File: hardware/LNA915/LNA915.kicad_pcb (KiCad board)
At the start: 4 copper layers, 38 x 7.8 mm, 32 parts, among them P1 HACKRF, P2 ANTENNA, U1 SWITCH, U2 SAW, U3 LNA

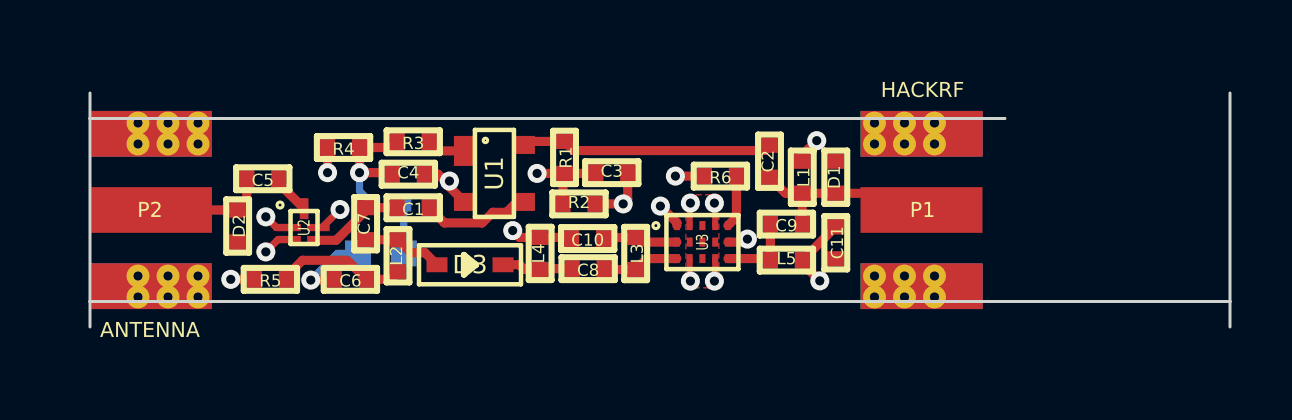
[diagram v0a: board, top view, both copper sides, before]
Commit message: LNA915: correct minor layout errors
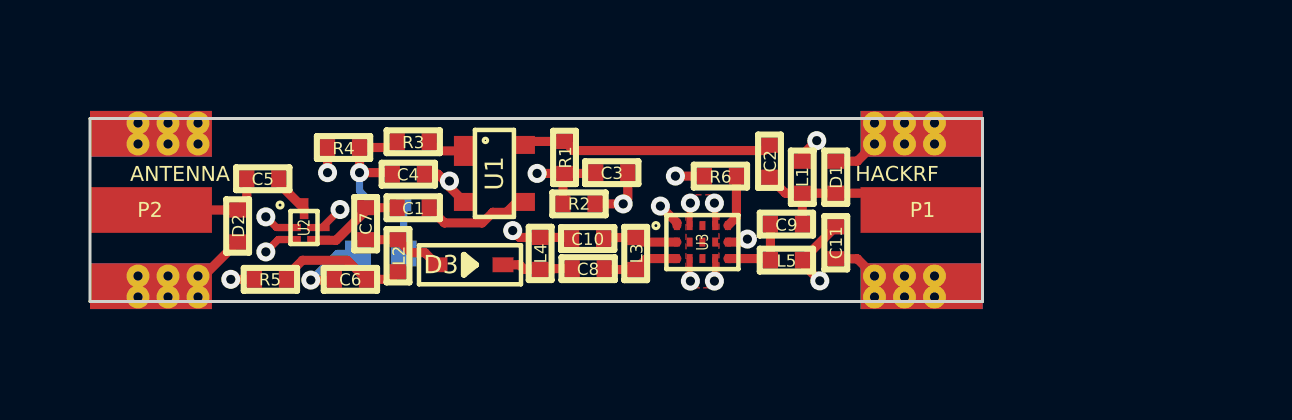
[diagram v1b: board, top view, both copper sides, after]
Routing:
- net GND: track 15.5 -> 21.3 mm
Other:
- board size 38 x 7.8 mm -> 29.8 x 6.1 mm
- board text added: "21 Jun 2020"
- board text added: "https://greatscottgadgets.com/"
- board text removed: "11 Jan 2016"
- board text removed: "http://greatscottgadgets.com/hackrf/"

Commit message: LNA915: redesign around GRF6011 failsafe switch
fits in SMA-KIT-1.5MF inline SMA enclosure
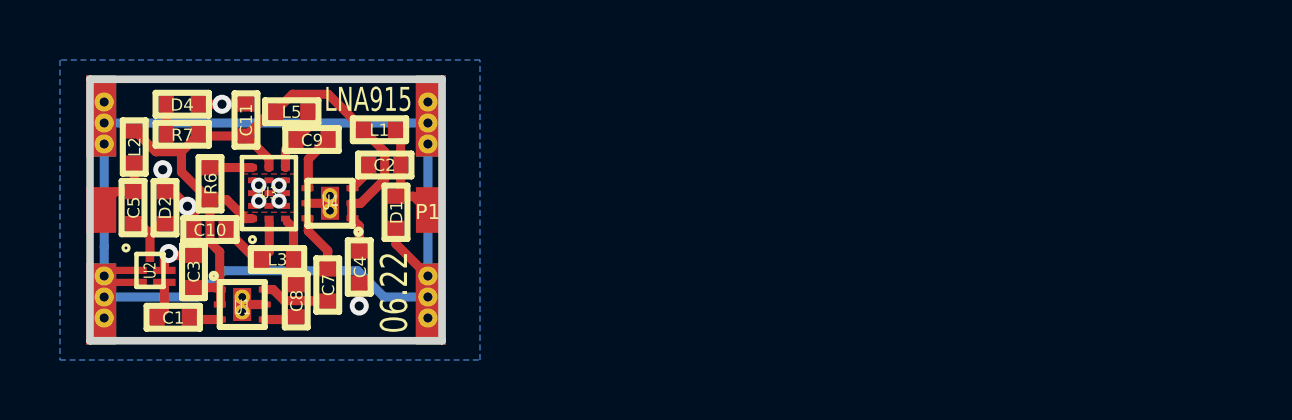
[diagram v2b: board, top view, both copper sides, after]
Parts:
- removed C6: 1nF, gsg-modules:0402
- removed D3: PIN, hackrf:GSG-SOD323
- removed L4: 39nH, gsg-modules:0402
- removed P2: ANTENNA, gsg-modules:SMA-EDGE
- removed R1: 47k, gsg-modules:0402
- removed R2, R4: 100k, gsg-modules:0402
- removed R3: 4k7, gsg-modules:0402
- removed R5: 470, gsg-modules:0402
- added U4: SWITCH, LNA915:GRF6011, F.Cu at (133.0, 99.8)
- C3, C4: value 1nF -> 100pF
- D4: footprint gsg-modules:0603D -> gsg-modules:0402; moved to F.Cu
- P1: value HACKRF -> SMA-KIT-1.5MF; footprint gsg-modules:SMA-EDGE -> LNA915:SMA-KIT-1.5MF
- R7: moved to F.Cu
- U1: footprint hackrf:GSG-SOT143 -> LNA915:GRF6011
- moved C11 20.1 mm to (130.2, 97.0), turned to 270 degrees
- moved P1 17.9 mm to (136.9, 100.0)
- moved L5 17.2 mm to (131.7, 96.7), turned to 0 degrees
- moved R6 17.0 mm to (129.0, 99.1), turned to 90 degrees
- moved C9 16.1 mm to (132.4, 97.7)
- moved D1 14.7 mm to (135.2, 100.1), turned to 90 degrees
- moved U3 14.5 mm to (131.0, 99.4), turned to 0 degrees
- moved C3 14.3 mm to (128.4, 102.0), turned to 270 degrees
- moved L1 14.2 mm to (134.7, 97.3), turned to 180 degrees
- moved C2 12.8 mm to (134.8, 98.5), turned to 0 degrees
- moved C10 12.6 mm to (129.0, 100.7)
- moved L3 11.9 mm to (131.2, 101.7), turned to 180 degrees
- moved C8 9.79 mm to (131.9, 103.0), turned to 90 degrees
- moved L2 9.51 mm to (126.5, 97.9), turned to 90 degrees
- moved U1 9.47 mm to (130.1, 103.2), turned to 0 degrees
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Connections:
- C7 pad 1: Net-(C1-Pad1) -> Net-(C7-Pad1)
- C9 pad 2: Net-(C2-Pad2) -> Net-(C9-Pad2)
- D2 pad 2: Net-(C5-Pad1) -> Net-(C5-Pad2)
- D4 pad 1: Net-(D4-Pad1) -> GND
- D4 pad 2: GND -> Net-(D4-Pad2)
- L2 pad 1: Net-(C7-Pad2) -> Net-(C5-Pad1)
- L2 pad 2: Net-(C6-Pad2) -> VCC
- R7 pad 2: Net-(D4-Pad1) -> Net-(D4-Pad2)
- U1 pad 1: Net-(R3-Pad2) -> VCC
- U1 pad 2: GND -> VCC
- U1 pad 4: Net-(C2-Pad1) -> Net-(C8-Pad1)
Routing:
- net GND: track 21.3 -> 51.5 mm, vias 12 -> 9
- net VCC: track 14.0 -> 24.0 mm, vias 8 -> 0
- net Net-(C2-Pad1): track 8.42 -> 1.01 mm
- net Net-(C6-Pad2): track 4.41 -> 0.00 mm
- net Net-(C2-Pad2): track 6.56 -> 3.67 mm
- net Net-(C1-Pad2): track 3.67 -> 1.07 mm
- net Net-(C7-Pad1): track 0.00 -> 2.29 mm
- net Net-(C1-Pad1): track 3.13 -> 1.15 mm
- net Net-(C9-Pad2): track 0.00 -> 1.90 mm
- net Net-(C5-Pad1): track 4.06 -> 2.35 mm
- net Net-(D4-Pad1): track 1.68 -> 0.00 mm
- net Net-(C8-Pad1): track 2.42 -> 1.11 mm
- net Net-(R3-Pad2): track 1.30 -> 0.00 mm
- net Net-(D4-Pad2): track 0.00 -> 1.00 mm
- net Net-(C7-Pad2): track 2.72 -> 1.96 mm
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- added copper zone on B.Cu, net GND
- removed copper zone on C2, net GND
- removed copper zone on C3, net VCC
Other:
- board size 29.8 x 6.1 mm -> 11.7 x 8.7 mm
- copper layers 4 -> 2
- net class Default: clearance 0.1524 -> 0.127
- rule pad_to_mask_clearance: 0.0762 -> 0.0508
- rule trace_clearance: 0.1524 -> 0.127
- board text added: "06.22"
- board text added: "RX"
- board text added: "TX"
- board text removed: "21 Jun 2020"
- board text removed: "LNA"
- board text removed: "P1"
- board text removed: "P2"
- board text removed: "https://greatscottgadgets.com/"

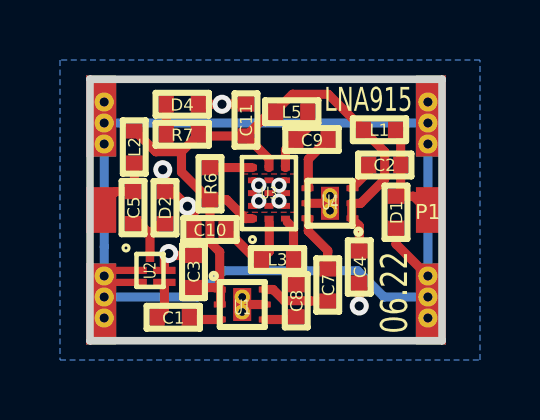
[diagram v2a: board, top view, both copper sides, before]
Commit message: LNA915: make easier to assemble
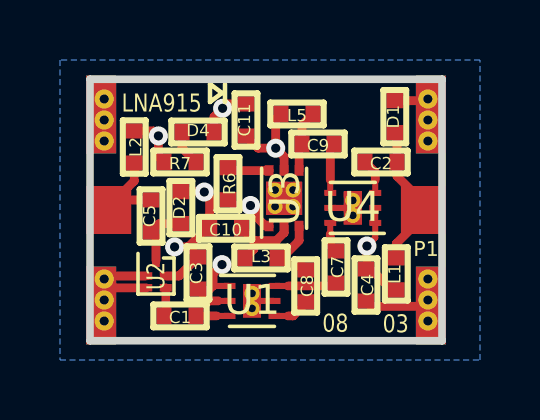
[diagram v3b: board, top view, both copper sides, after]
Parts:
- U2: footprint hackrf:GSG-F5Q -> LNA915:F5Q
- U3: footprint hackrf:GSG-TSLP-7-1 -> LNA915:TSLP-7-1
- moved L1 4.84 mm to (135.2, 102.1), turned to 270 degrees
- moved D1 3.19 mm to (135.2, 96.9), turned to 270 degrees
- moved D4 1.06 mm to (128.6, 97.4)
- moved R7 0.93 mm to (128.0, 98.4), turned to 0 degrees
- moved U4 0.78 mm to (133.8, 99.9)
- moved C5 0.66 mm to (127.0, 100.2)
- moved C7 0.66 mm to (133.2, 101.9)
- moved C4 0.64 mm to (134.2, 102.5)
- moved R6 0.60 mm to (129.6, 99.1)
- moved C8 0.59 mm to (132.2, 102.5)
- moved L3 0.55 mm to (130.7, 101.6)
- moved U3 0.53 mm to (131.5, 99.6)
- moved D2 0.53 mm to (128.0, 99.9)
- moved C10 0.52 mm to (129.5, 100.6)
- moved U1 0.35 mm to (130.4, 103.0)
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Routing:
- net GND: track 51.5 -> 14.9 mm, vias 9 -> 3
- net VCC: track 24.0 -> 13.6 mm, vias 0 -> 5
- net Net-(C2-Pad2): track 3.67 -> 5.23 mm
- net Net-(C5-Pad1): track 2.35 -> 3.47 mm
- net Net-(C7-Pad2): track 1.96 -> 1.02 mm
- added copper zone on In1.Cu, net GND
- added copper zone on In2.Cu, net VCC
- removed copper zone on F.Cu, net GND
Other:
- copper layers 2 -> 4
- net class Default: trace_width 0.1524 -> 0.29337
- board text added: "03"
- board text added: "08"
- board text removed: "06.22"

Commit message: LNA915: add optional shunt capacitor
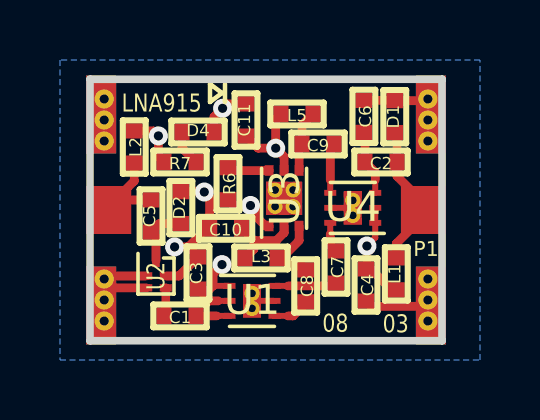
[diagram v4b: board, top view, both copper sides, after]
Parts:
- added C6: 1 pF, gsg-modules:0402, F.Cu at (134.1, 96.9)
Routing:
- net GND: track 14.9 -> 15.9 mm
- net Net-(C2-Pad1): track 1.17 -> 2.17 mm

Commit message: LNA915: renumber reference designators
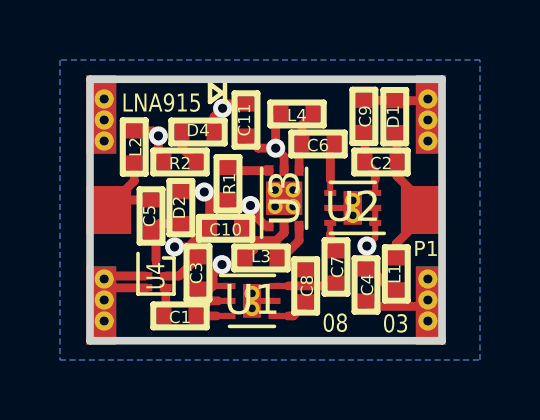
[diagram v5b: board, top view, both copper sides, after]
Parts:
- renumbered C9 to C6, C6 to C9, L5 to L4, R6 to R1, R7 to R2, U4 to U2, U2 to U4
